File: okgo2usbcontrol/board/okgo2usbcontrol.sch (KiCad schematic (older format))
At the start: 22 parts, among them IC1 ADP3335, IC2 STM32F042K6T6, P1 USB-A, P2 SWD_TC, P3 COAX, SW1 FIRE, SW2 ARM, U1 RFM95W

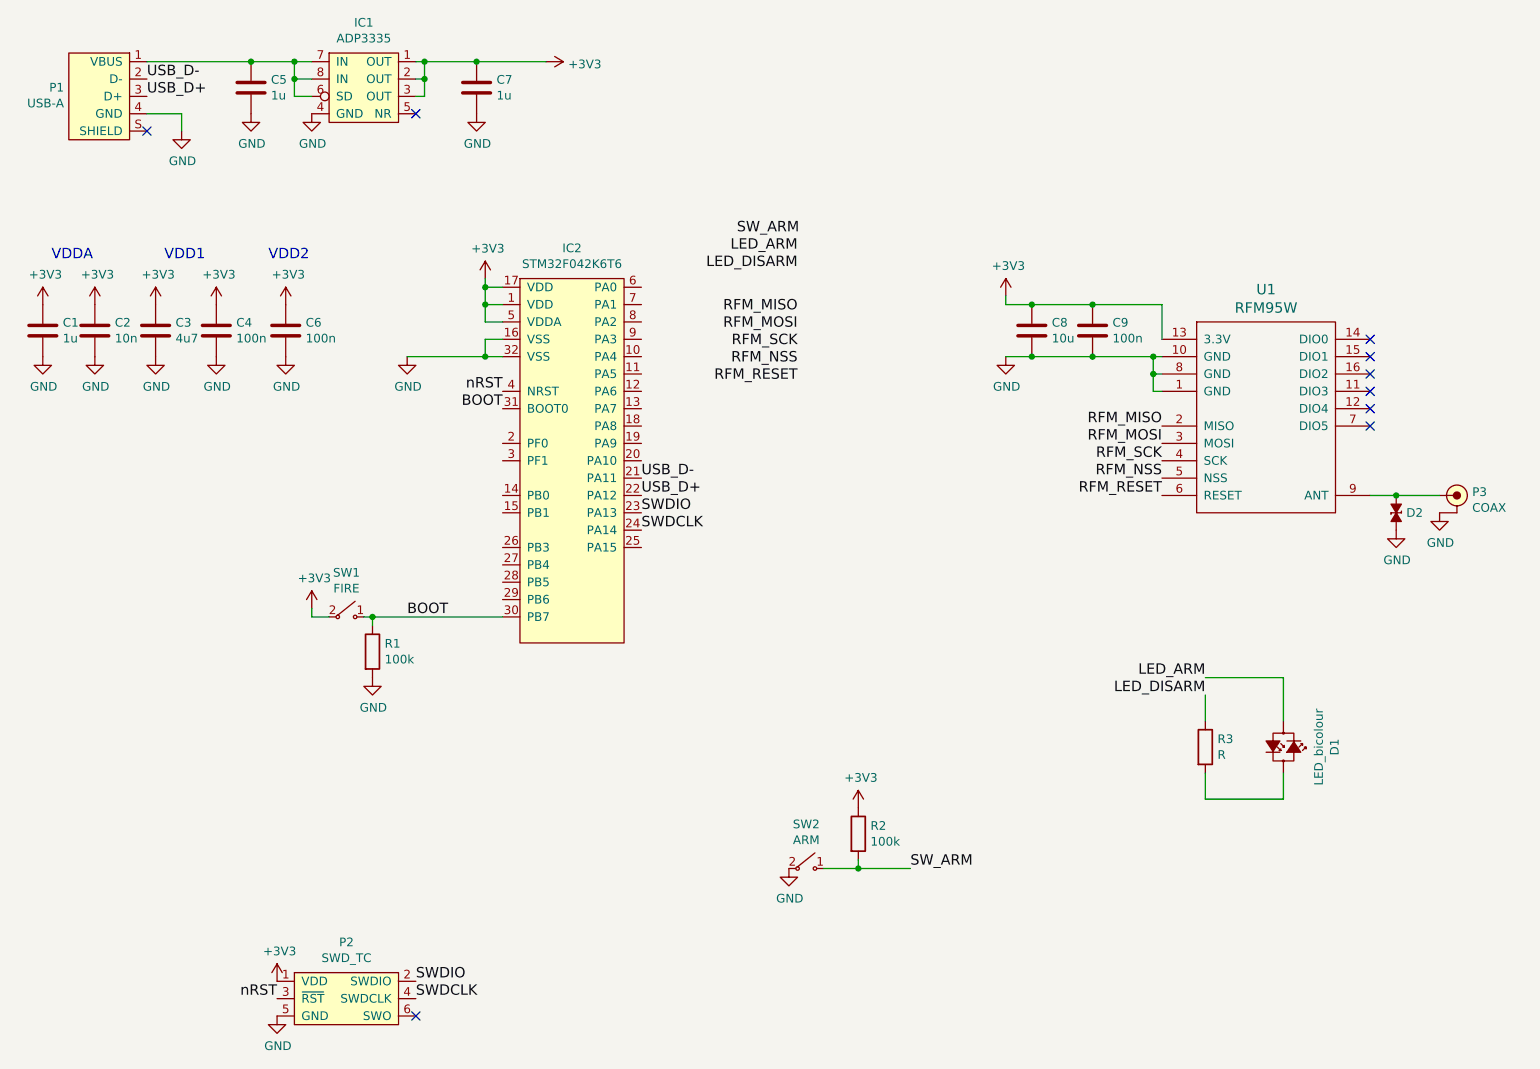
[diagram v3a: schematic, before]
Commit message: Tweak usbcontrol into silly dongle board
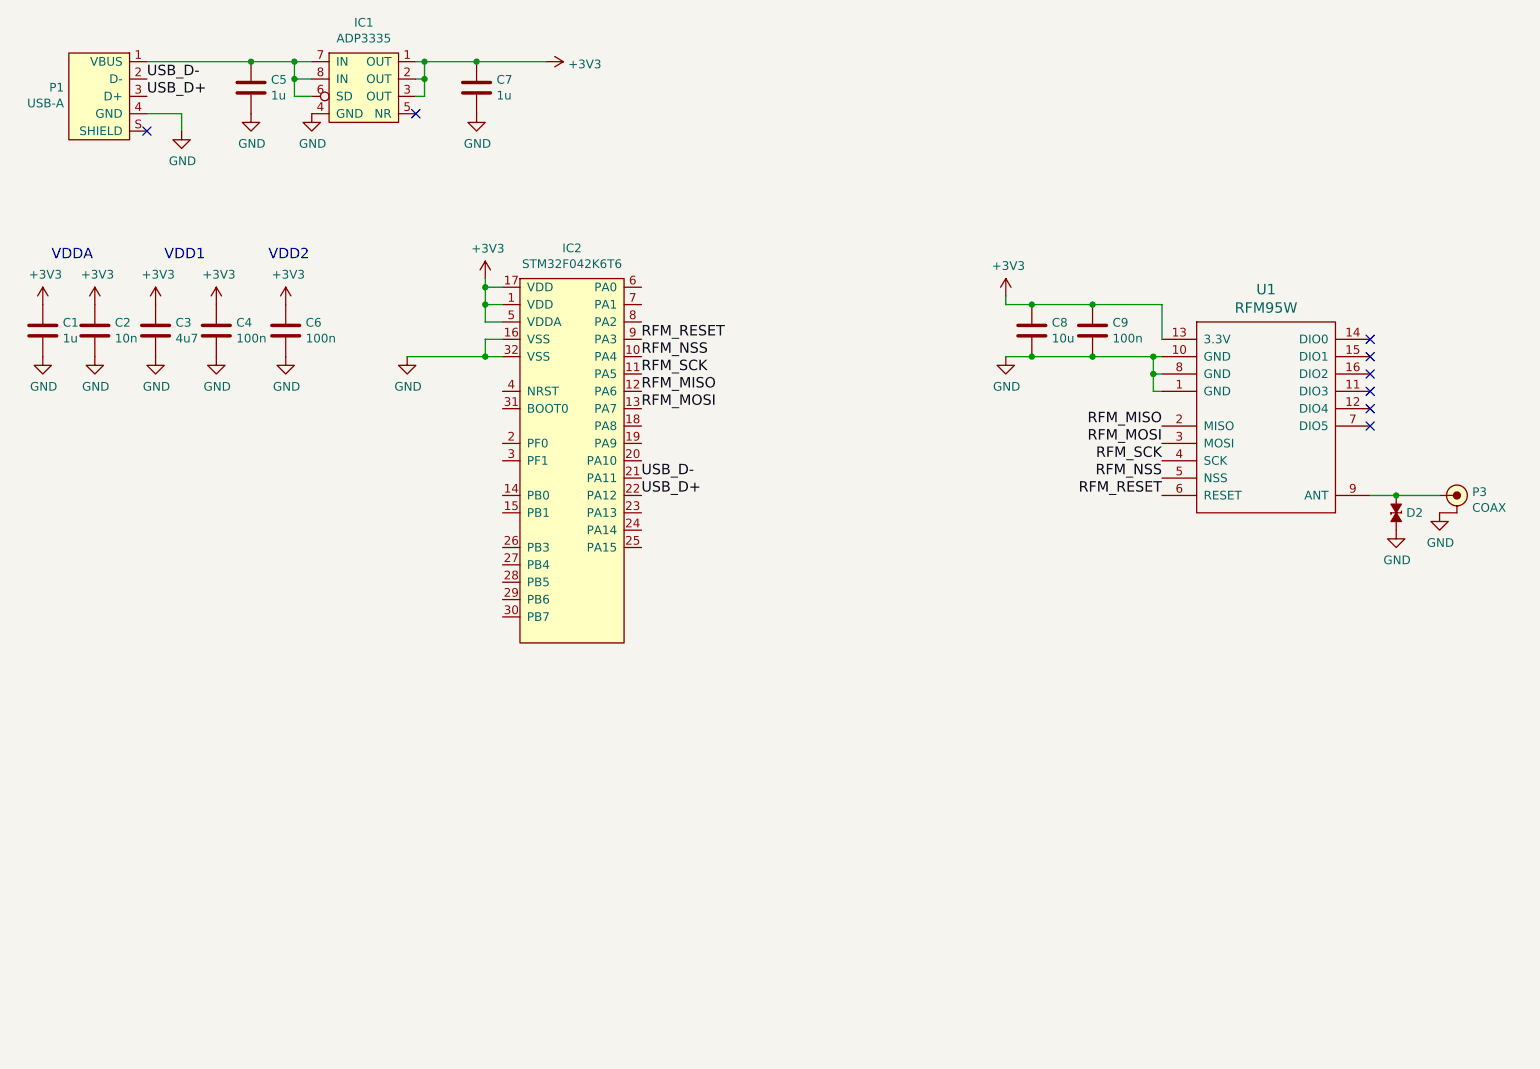
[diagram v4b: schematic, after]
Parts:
- removed D1: LED_bicolour, agg:0805-LED, symbol LED_bicolour
- removed P2: SWD_TC, agg:TC2030-NL, symbol SWD_TC
- removed R1, R2: 100k, agg:0603, symbol R
- removed R3: R, agg:0603, symbol R
- removed SW1: FIRE, footprints:FSM2JSMx, symbol SWITCH_SPST
- removed SW2: ARM, footprints:JSX08001SAQNL, symbol SWITCH_SPST
- C1, C2, C3, C4, C5, C6, C7, C8, C9: footprint agg:0603 -> agg:0402
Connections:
- net RFM_MISO: now also IC2.12 (PA6)
- net RFM_MOSI: now also IC2.13 (PA7)
- net RFM_NSS: now also IC2.10 (PA4)
- net RFM_RESET: now also IC2.9 (PA3)
- net RFM_SCK: now also IC2.11 (PA5)
- net BOOT: no longer names the net of IC2.30 (PB7)
- net BOOT: no longer IC2.31 (BOOT0)
- net SWDCLK: no longer names the net of IC2.24 (PA14)
- net SWDIO: no longer names the net of IC2.23 (PA13)
- net nRST: no longer names the net of IC2.4 (NRST)
- no-connect marks 9 -> 8
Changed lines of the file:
@@
 LIBS:contrib
 LIBS:valves
-LIBS:coax
 LIBS:okgo2usbcontrol-cache
 EELAYER 26 0
@@
 $EndComp
 $Comp
-L SWD_TC P2
-U 1 1 59970189
-P 2700 6250
-F 0 "P2" H 2700 6575 50  0000 C CNN
-F 1 "SWD_TC" H 2700 6484 50  0000 C CNN
-F 2 "agg:TC2030-NL" H 2400 5950 50  0001 L CNN
-F 3 "" H 2300 6350 50  0001 C CNN
-	1    2700 6250
-	1    0    0    -1
-$EndComp
-$Comp
-L LED_bicolour D1
-U 1 1 59970259
-P 8100 4800
-F 0 "D1" H 8100 5095 50  0000 C CNN
-F 1 "LED_bicolour" H 8100 5004 50  0000 C CNN
-F 2 "agg:0805-LED" V 8100 4860 60  0001 C CNN
-F 3 "" V 8100 4860 60  0000 C CNN
-	1    8100 4800
-	0    1    1    0
-$EndComp
-$Comp
 L RFM95W U1
 U 1 1 599702C4
@@
 	1    0    0    -1
 $EndComp
-$Comp
-L SWITCH_SPST SW1
-U 1 1 599705A2
-P 2700 4050
-F 0 "SW1" H 2700 4305 50  0000 C CNN
-F 1 "FIRE" H 2700 4214 50  0000 C CNN
-F 2 "footprints:FSM2JSMx" H 2700 4050 50  0001 C CNN
-F 3 "http://www.farnell.com/datasheets/2074946.pdf" H 2700 4050 50  0001 C CNN
-F 4 "2610947" H 2700 4050 60  0001 C CNN "Farnell"
-	1    2700 4050
-	1    0    0    -1
-$EndComp
-$Comp
-L SWITCH_SPST SW2
-U 1 1 59970728
-P 5350 5500
-F 0 "SW2" H 5350 5755 50  0000 C CNN
-F 1 "ARM" H 5350 5664 50  0000 C CNN
-F 2 "footprints:JSX08001SAQNL" H 5350 5500 50  0001 C CNN
-F 3 "http://www.farnell.com/datasheets/1839855.pdf" H 5350 5500 50  0001 C CNN
-F 4 "2435152" H 5350 5500 60  0001 C CNN "Farnell"
-	1    5350 5500
-	1    0    0    -1
-$EndComp
-$Comp
-L +3V3 #PWR01
-U 1 1 59971DC0
-P 2500 4000
-F 0 "#PWR01" H 2500 3850 50  0001 C CNN
-F 1 "+3V3" H 2515 4173 50  0000 C CNN
-F 2 "" H 2500 4000 50  0001 C CNN
-F 3 "" H 2500 4000 50  0001 C CNN
-	1    2500 4000
-	1    0    0    -1
-$EndComp
-Wire Wire Line
-	2500 4000 2500 4050
-Wire Wire Line
-	2500 4050 2600 4050
-$Comp
-L R R1
-U 1 1 59971E13
-P 2850 4250
-F 0 "R1" H 2920 4296 50  0000 L CNN
-F 1 "100k" H 2920 4205 50  0000 L CNN
-F 2 "agg:0603" V 2780 4250 50  0001 C CNN
-F 3 "" H 2850 4250 50  0001 C CNN
-	1    2850 4250
-	1    0    0    -1
-$EndComp
-Wire Wire Line
-	2800 4050 3600 4050
-Wire Wire Line
-	2850 4050 2850 4100
-Connection ~ 2850 4050
-Text Label 3050 4050 0    60   ~ 0
-BOOT
-$Comp
-L GND #PWR02
-U 1 1 59972159
-P 2850 4400
-F 0 "#PWR02" H 2850 4150 50  0001 C CNN
-F 1 "GND" H 2855 4227 50  0000 C CNN
-F 2 "" H 2850 4400 50  0001 C CNN
-F 3 "" H 2850 4400 50  0001 C CNN
-	1    2850 4400
-	1    0    0    -1
-$EndComp
-Text Label 3600 2850 2    60   ~ 0
-BOOT
 Text Label 1550 950  0    60   ~ 0
 USB_D-
@@
 F 0 "C5" H 2265 1046 50  0000 L CNN
 F 1 "1u" H 2265 955 50  0000 L CNN
-F 2 "agg:0603" H 2188 850 50  0001 C CNN
+F 2 "agg:0402" H 2188 850 50  0001 C CNN
 F 3 "" H 2150 1000 50  0001 C CNN
 	1    2150 1000
@@
 F 0 "C7" H 3565 1046 50  0000 L CNN
 F 1 "1u" H 3565 955 50  0000 L CNN
-F 2 "agg:0603" H 3488 850 50  0001 C CNN
+F 2 "agg:0402" H 3488 850 50  0001 C CNN
 F 3 "" H 3450 1000 50  0001 C CNN
 	1    3450 1000
@@
 	0    1    1    0
 $EndComp
-$Comp
-L +3V3 #PWR08
-U 1 1 59973895
-P 2300 6150
-F 0 "#PWR08" H 2300 6000 50  0001 C CNN
-F 1 "+3V3" H 2315 6323 50  0000 C CNN
-F 2 "" H 2300 6150 50  0001 C CNN
-F 3 "" H 2300 6150 50  0001 C CNN
-	1    2300 6150
-	1    0    0    -1
-$EndComp
-$Comp
-L GND #PWR09
-U 1 1 59973BD8
-P 2300 6350
-F 0 "#PWR09" H 2300 6100 50  0001 C CNN
-F 1 "GND" H 2305 6177 50  0000 C CNN
-F 2 "" H 2300 6350 50  0001 C CNN
-F 3 "" H 2300 6350 50  0001 C CNN
-	1    2300 6350
-	1    0    0    -1
-$EndComp
-Text Label 2300 6250 2    60   ~ 0
-nRST
-Text Label 3100 6150 0    60   ~ 0
-SWDIO
-Text Label 3100 6250 0    60   ~ 0
-SWDCLK
-NoConn ~ 3100 6350
-Text Label 4400 3450 0    60   ~ 0
-SWDIO
-Text Label 4400 3550 0    60   ~ 0
-SWDCLK
-Text Label 3600 2750 2    60   ~ 0
-nRST
 Text Label 4400 3250 0    60   ~ 0
 USB_D-
@@
 F 0 "C9" H 7115 2446 50  0000 L CNN
 F 1 "100n" H 7115 2355 50  0000 L CNN
-F 2 "agg:0603" H 7038 2250 50  0001 C CNN
+F 2 "agg:0402" H 7038 2250 50  0001 C CNN
 F 3 "" H 7000 2400 50  0001 C CNN
 	1    7000 2400
@@
 F 0 "C8" H 6765 2446 50  0000 L CNN
 F 1 "10u" H 6765 2355 50  0000 L CNN
-F 2 "agg:0603" H 6688 2250 50  0001 C CNN
+F 2 "agg:0402" H 6688 2250 50  0001 C CNN
 F 3 "" H 6650 2400 50  0001 C CNN
 	1    6650 2400
@@
 Text Label 7400 3350 2    60   ~ 0
 RFM_RESET
-Text Label 5300 2300 2    60   ~ 0
+Text Label 4400 2750 0    60   ~ 0
 RFM_MISO
-Text Label 5300 2400 2    60   ~ 0
+Text Label 4400 2850 0    60   ~ 0
 RFM_MOSI
-Text Label 5300 2500 2    60   ~ 0
+Text Label 4400 2650 0    60   ~ 0
 RFM_SCK
-Text Label 5300 2600 2    60   ~ 0
+Text Label 4400 2550 0    60   ~ 0
 RFM_NSS
-Text Label 5300 2700 2    60   ~ 0
+Text Label 4400 2450 0    60   ~ 0
 RFM_RESET
-$Comp
-L GND #PWR014
-U 1 1 5997659A
-P 5250 5500
-F 0 "#PWR014" H 5250 5250 50  0001 C CNN
-F 1 "GND" H 5255 5327 50  0000 C CNN
-F 2 "" H 5250 5500 50  0001 C CNN
-F 3 "" H 5250 5500 50  0001 C CNN
-	1    5250 5500
-	1    0    0    -1
-$EndComp
-$Comp
-L R R2
-U 1 1 5997671C
-P 5650 5300
-F 0 "R2" H 5720 5346 50  0000 L CNN
-F 1 "100k" H 5720 5255 50  0000 L CNN
-F 2 "agg:0603" V 5580 5300 50  0001 C CNN
-F 3 "" H 5650 5300 50  0001 C CNN
-	1    5650 5300
-	1    0    0    -1
-$EndComp
-$Comp
-L +3V3 #PWR015
-U 1 1 5997679F
-P 5650 5150
-F 0 "#PWR015" H 5650 5000 50  0001 C CNN
-F 1 "+3V3" H 5665 5323 50  0000 C CNN
-F 2 "" H 5650 5150 50  0001 C CNN
-F 3 "" H 5650 5150 50  0001 C CNN
-	1    5650 5150
-	1    0    0    -1
-$EndComp
-Wire Wire Line
-	5650 5450 5650 5500
-Wire Wire Line
-	5450 5500 5950 5500
-Connection ~ 5650 5500
-Text Label 5950 5500 0    60   ~ 0
-SW_ARM
-$Comp
-L R R3
-U 1 1 599772FC
-P 7650 4800
-F 0 "R3" H 7720 4846 50  0000 L CNN
-F 1 "R" H 7720 4755 50  0000 L CNN
-F 2 "agg:0603" V 7580 4800 50  0001 C CNN
-F 3 "" H 7650 4800 50  0001 C CNN
-	1    7650 4800
-	1    0    0    -1
-$EndComp
-Text Label 7650 4400 2    60   ~ 0
-LED_ARM
-Text Label 7650 4500 2    60   ~ 0
-LED_DISARM
-Wire Wire Line
-	7650 4500 7650 4650
-Wire Wire Line
-	7650 4400 8100 4400
-Wire Wire Line
-	8100 4400 8100 4650
-Text Label 4950 1850 0    60   ~ 0
-SW_ARM
-Text Label 5300 1950 2    60   ~ 0
-LED_ARM
-Text Label 5300 2050 2    60   ~ 0
-LED_DISARM
 $Comp
 L +3V3 #PWR016
@@
 F 0 "C1" H 1065 2446 50  0000 L CNN
 F 1 "1u" H 1065 2355 50  0000 L CNN
-F 2 "agg:0603" H 988 2250 50  0001 C CNN
+F 2 "agg:0402" H 988 2250 50  0001 C CNN
 F 3 "" H 950 2400 50  0001 C CNN
 	1    950  2400
@@
 F 0 "C2" H 1365 2446 50  0000 L CNN
 F 1 "10n" H 1365 2355 50  0000 L CNN
-F 2 "agg:0603" H 1288 2250 50  0001 C CNN
+F 2 "agg:0402" H 1288 2250 50  0001 C CNN
 F 3 "" H 1250 2400 50  0001 C CNN
 	1    1250 2400
@@
 F 0 "C3" H 1715 2446 50  0000 L CNN
 F 1 "4u7" H 1715 2355 50  0000 L CNN
-F 2 "agg:0603" H 1638 2250 50  0001 C CNN
+F 2 "agg:0402" H 1638 2250 50  0001 C CNN
 F 3 "" H 1600 2400 50  0001 C CNN
 	1    1600 2400
@@
 F 0 "C4" H 2065 2446 50  0000 L CNN
 F 1 "100n" H 2065 2355 50  0000 L CNN
-F 2 "agg:0603" H 1988 2250 50  0001 C CNN
+F 2 "agg:0402" H 1988 2250 50  0001 C CNN
 F 3 "" H 1950 2400 50  0001 C CNN
 	1    1950 2400
@@
 F 0 "C6" H 2465 2446 50  0000 L CNN
 F 1 "100n" H 2465 2355 50  0000 L CNN
-F 2 "agg:0603" H 2388 2250 50  0001 C CNN
+F 2 "agg:0402" H 2388 2250 50  0001 C CNN
 F 3 "" H 2350 2400 50  0001 C CNN
 	1    2350 2400
@@
 Text Notes 2250 2000 0    60   ~ 0
 VDD2
-Wire Wire Line
-	7650 4950 7650 5100
-Wire Wire Line
-	7650 5100 8100 5100
-Wire Wire Line
-	8100 5100 8100 4950
 $Comp
 L COAX P3

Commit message: WIP
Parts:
- added R1: 100K, agg:0402, symbol R
- added W1: BOOT, agg:TESTPAD, symbol TEST_1P
- added W2: 3v3, agg:TESTPAD, symbol TEST_1P
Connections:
- net +3V3: now also W2.1
- net GND: now also R1.2
- net at IC2.31 (BOOT0): now also R1.1, W1.1
- no-connect marks 8 -> 27
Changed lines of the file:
@@
 	1    0    0    -1
 $EndComp
+$Comp
+L TEST_1P W1
+U 1 1 59A01B7D
+P 3350 2850
+F 0 "W1" V 3545 2924 50  0001 C CNN
+F 1 "BOOT" V 3350 3150 50  0000 C CNN
+F 2 "agg:TESTPAD" H 3550 2850 50  0001 C CNN
+F 3 "" H 3550 2850 50  0000 C CNN
+	1    3350 2850
+	0    -1   -1   0
+$EndComp
+NoConn ~ 3600 2750
+NoConn ~ 3600 3050
+NoConn ~ 3600 3150
+NoConn ~ 3600 3350
+NoConn ~ 3600 3450
+NoConn ~ 3600 3650
+NoConn ~ 3600 3750
+NoConn ~ 3600 3850
+NoConn ~ 3600 3950
+NoConn ~ 3600 4050
+NoConn ~ 4400 3650
+NoConn ~ 4400 3550
+NoConn ~ 4400 3450
+NoConn ~ 4400 3150
+NoConn ~ 4400 3050
+NoConn ~ 4400 2950
+NoConn ~ 4400 2150
+NoConn ~ 4400 2250
+NoConn ~ 4400 2350
+$Comp
+L R R1
+U 1 1 59A0286A
+P 3350 3000
+F 0 "R1" H 3150 3050 50  0000 L CNN
+F 1 "100K" H 3100 2950 50  0000 L CNN
+F 2 "agg:0402" V 3280 3000 50  0001 C CNN
+F 3 "" H 3350 3000 50  0000 C CNN
+	1    3350 3000
+	1    0    0    -1
+$EndComp
+$Comp
+L GND #PWR01
+U 1 1 59A029A2
+P 3350 3150
+F 0 "#PWR01" H 3350 2900 50  0001 C CNN
+F 1 "GND" H 3355 2977 50  0000 C CNN
+F 2 "" H 3350 3150 50  0001 C CNN
+F 3 "" H 3350 3150 50  0001 C CNN
+	1    3350 3150
+	1    0    0    -1
+$EndComp
+Wire Wire Line
+	3600 2850 3350 2850
+Connection ~ 3350 2850
+$Comp
+L TEST_1P W2
+U 1 1 59A02A1A
+P 3500 2150
+F 0 "W2" V 3695 2224 50  0001 C CNN
+F 1 "3v3" V 3500 2450 50  0000 C CNN
+F 2 "agg:TESTPAD" H 3700 2150 50  0001 C CNN
+F 3 "" H 3700 2150 50  0000 C CNN
+	1    3500 2150
+	0    -1   -1   0
+$EndComp
 $EndSCHEMATC

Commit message: WIP
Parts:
- W1, W2: footprint agg:TESTPAD -> footprints:PokyPad
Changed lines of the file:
@@
 F 0 "W1" V 3545 2924 50  0001 C CNN
 F 1 "BOOT" V 3350 3150 50  0000 C CNN
-F 2 "agg:TESTPAD" H 3550 2850 50  0001 C CNN
+F 2 "footprints:PokyPad" H 3550 2850 50  0001 C CNN
 F 3 "" H 3550 2850 50  0000 C CNN
 	1    3350 2850
@@
 F 0 "W2" V 3695 2224 50  0001 C CNN
 F 1 "3v3" V 3500 2450 50  0000 C CNN
-F 2 "agg:TESTPAD" H 3700 2150 50  0001 C CNN
+F 2 "footprints:PokyPad" H 3700 2150 50  0001 C CNN
 F 3 "" H 3700 2150 50  0000 C CNN
 	1    3500 2150
